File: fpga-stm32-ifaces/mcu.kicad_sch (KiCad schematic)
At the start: 58 parts, among them J10 CORTEX_DEBUG_ETM, J3 PMOD_HOST, J4 XILINX_JTAG, J5 CONN_01X03, U1 STM32H735-UFBGA176-25, U16 W25Q128JV, U2 XC7S25-1FTGB196, U8 AT24MAC402, U9 ECS-1612MV-250-CN

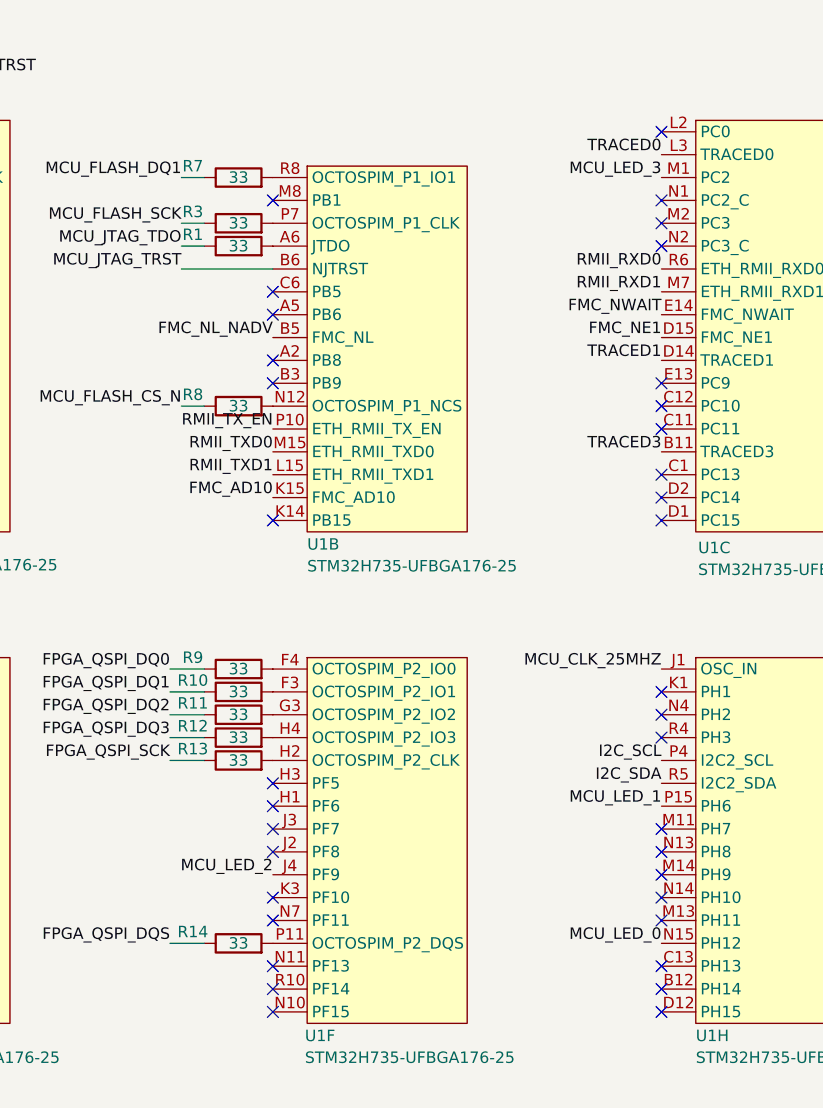
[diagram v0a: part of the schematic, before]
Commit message: Finished initial layout, passing DRC
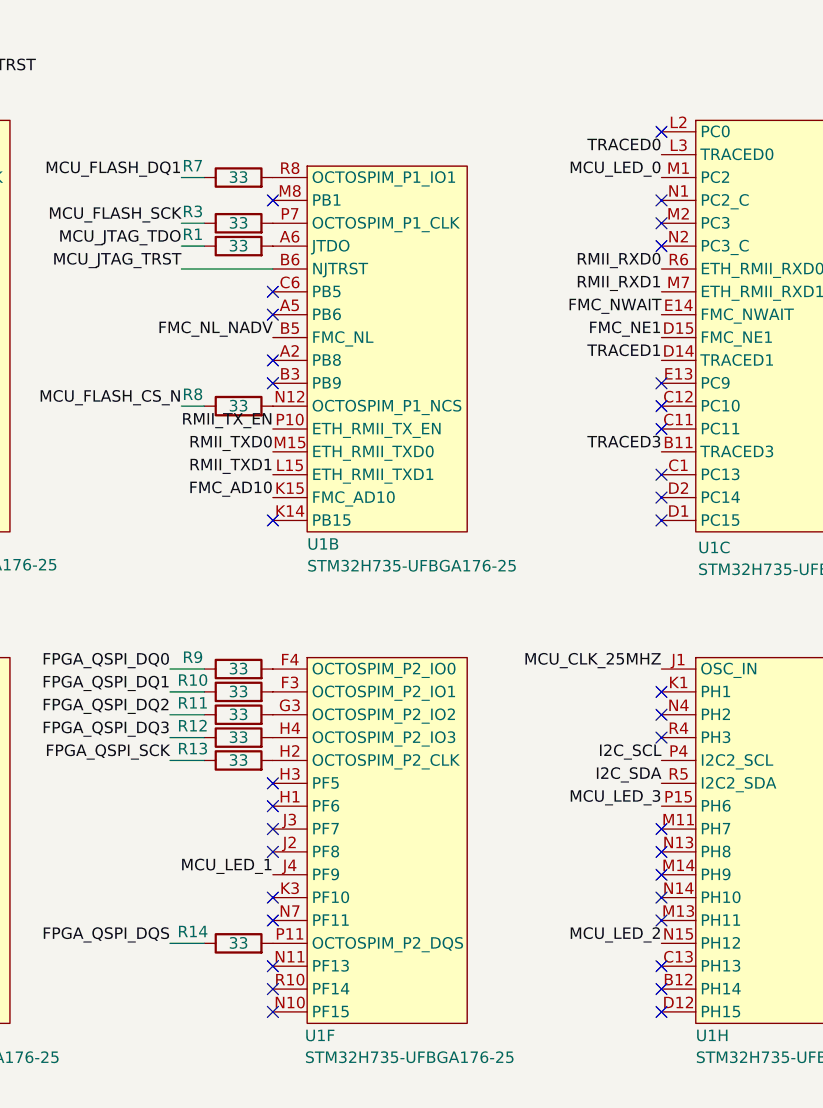
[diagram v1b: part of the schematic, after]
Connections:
- net MCU_LED_0: now also U1.M1 (PC2); no longer U1.N15 (PH12)
- net MCU_LED_1: now also U1.J4 (PF9); no longer U1.P15 (PH6)
- net MCU_LED_2: now also U1.N15 (PH12); no longer U1.J4 (PF9)
- net MCU_LED_3: now also U1.P15 (PH6); no longer U1.M1 (PC2)
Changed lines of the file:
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@@
 	)
 	(label "MCU_LED_2"
-		(at 91.44 113.03 180)
+		(at 134.62 120.65 180)
 		(fields_autoplaced yes)
 		(effects
@@
 	)
 	(label "MCU_LED_3"
-		(at 134.62 35.56 180)
+		(at 134.62 105.41 180)
 		(fields_autoplaced yes)
 		(effects
@@
 	)
 	(label "MCU_LED_0"
-		(at 134.62 120.65 180)
+		(at 134.62 35.56 180)
 		(fields_autoplaced yes)
 		(effects
@@
 	)
 	(label "MCU_LED_1"
-		(at 134.62 105.41 180)
-		(fields_autoplaced yes)
-		(effects
+		(at 91.44 113.03 180)
+		(fields_autoplaced yes)
+		(effects

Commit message: Lots of routing cleanup
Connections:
- net FMC_AD5: now also U2.J4 (IO_L17P_T2_34); no longer U2.J3 (IO_L17N_T2_34)
- net FMC_AD9: now also U2.M5 (IO_L23P_T3_34); no longer U2.K3 (IO_L16N_T2_34)
- net FMC_NL_NADV: now also U2.B2 (IO_L5P_T0_34); no longer U2.C1 (IO_L11N_T1_SRCC_34)
- net FPGA_QSPI_DQ4: now also U2.L5 (IO_25_34); no longer U2.M5 (IO_L23P_T3_34)
- net FPGA_QSPI_DQ5: now also U2.L3 (IO_L22P_T3_34); no longer U2.L5 (IO_25_34)
- net FPGA_QSPI_DQ7: now also U2.C1 (IO_L11N_T1_SRCC_34); no longer U2.B2 (IO_L5P_T0_34)
- net FPGA_QSPI_DQS: now also U2.K4 (IO_L16P_T2_34); no longer U2.L3 (IO_L22P_T3_34)
- net RMII_CRS_DV: now also U2.M4 (IO_L23N_T3_34); no longer U2.K4 (IO_L16P_T2_34)
- net RMII_RXD0: now also U2.K3 (IO_L16N_T2_34); no longer U2.M4 (IO_L23N_T3_34)
- net RMII_RXD1: now also U2.J3 (IO_L17N_T2_34); no longer U2.J4 (IO_L17P_T2_34)
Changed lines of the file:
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@@
 	)
 	(label "FPGA_QSPI_DQS"
-		(at 339.09 146.05 180)
+		(at 339.09 115.57 180)
 		(fields_autoplaced yes)
 		(effects
@@
 	)
 	(label "RMII_RXD1"
-		(at 339.09 120.65 180)
+		(at 339.09 123.19 180)
 		(fields_autoplaced yes)
 		(effects
@@
 	)
 	(label "RMII_RXD0"
-		(at 339.09 153.67 180)
+		(at 339.09 118.11 180)
 		(fields_autoplaced yes)
 		(effects
@@
 	)
 	(label "FMC_AD9"
-		(at 339.09 118.11 180)
+		(at 339.09 151.13 180)
 		(fields_autoplaced yes)
 		(effects
@@
 	)
 	(label "FPGA_QSPI_DQ7"
-		(at 339.09 59.69 180)
+		(at 339.09 92.71 180)
 		(fields_autoplaced yes)
 		(effects
@@
 	)
 	(label "FPGA_QSPI_DQ4"
-		(at 339.09 151.13 180)
+		(at 339.09 161.29 180)
 		(fields_autoplaced yes)
 		(effects
@@
 	)
 	(label "FMC_AD5"
-		(at 339.09 123.19 180)
+		(at 339.09 120.65 180)
 		(fields_autoplaced yes)
 		(effects
@@
 	)
 	(label "RMII_CRS_DV"
-		(at 339.09 115.57 180)
+		(at 339.09 153.67 180)
 		(fields_autoplaced yes)
 		(effects
@@
 	)
 	(label "FPGA_QSPI_DQ5"
-		(at 339.09 161.29 180)
+		(at 339.09 146.05 180)
 		(fields_autoplaced yes)
 		(effects
@@
 	)
 	(label "FMC_NL_NADV"
-		(at 339.09 92.71 180)
-		(fields_autoplaced yes)
-		(effects
+		(at 339.09 59.69 180)
+		(fields_autoplaced yes)
+		(effects

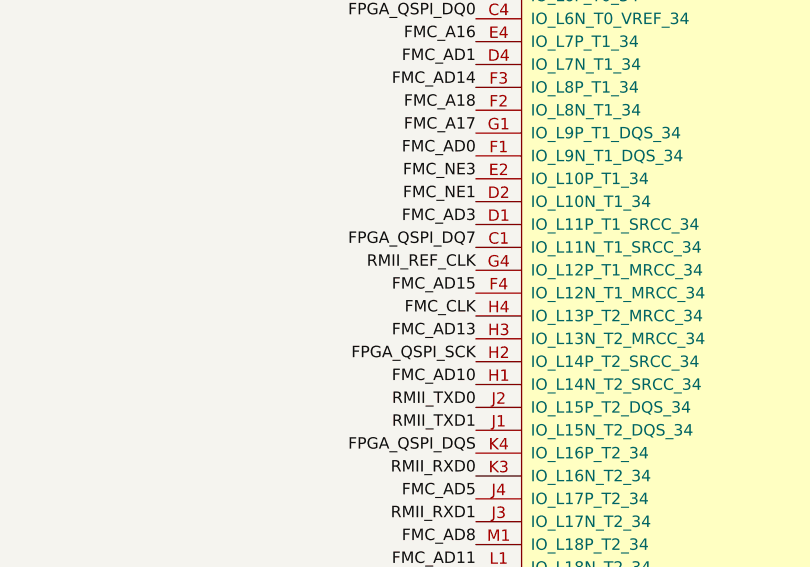
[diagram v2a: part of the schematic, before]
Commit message: More routing cleanup
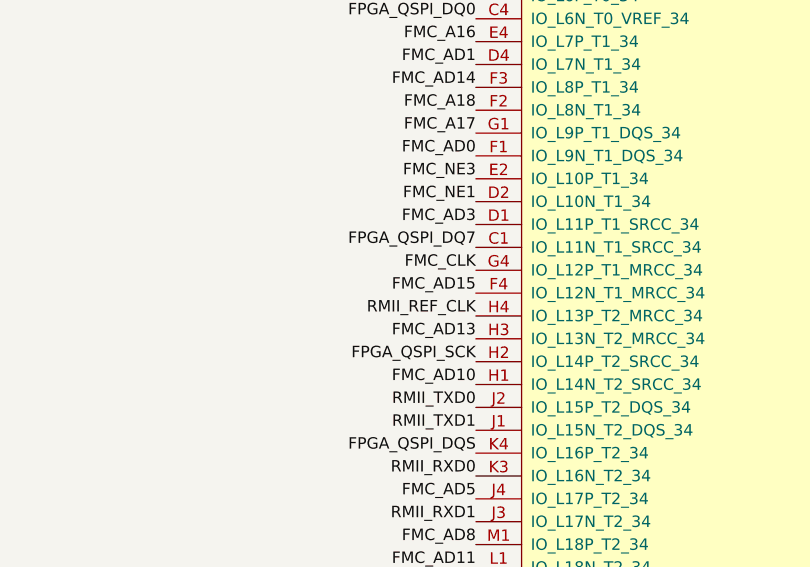
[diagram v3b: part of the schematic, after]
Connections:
- net FMC_CLK: now also U2.G4 (IO_L12P_T1_MRCC_34); no longer U2.H4 (IO_L13P_T2_MRCC_34)
- net RMII_REF_CLK: now also U2.H4 (IO_L13P_T2_MRCC_34); no longer U2.G4 (IO_L12P_T1_MRCC_34)
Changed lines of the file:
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@@
 	)
 	(label "RMII_REF_CLK"
-		(at 339.09 95.25 180)
+		(at 339.09 100.33 180)
 		(fields_autoplaced yes)
 		(effects
@@
 	)
 	(label "FMC_CLK"
-		(at 339.09 100.33 180)
-		(fields_autoplaced yes)
-		(effects
+		(at 339.09 95.25 180)
+		(fields_autoplaced yes)
+		(effects

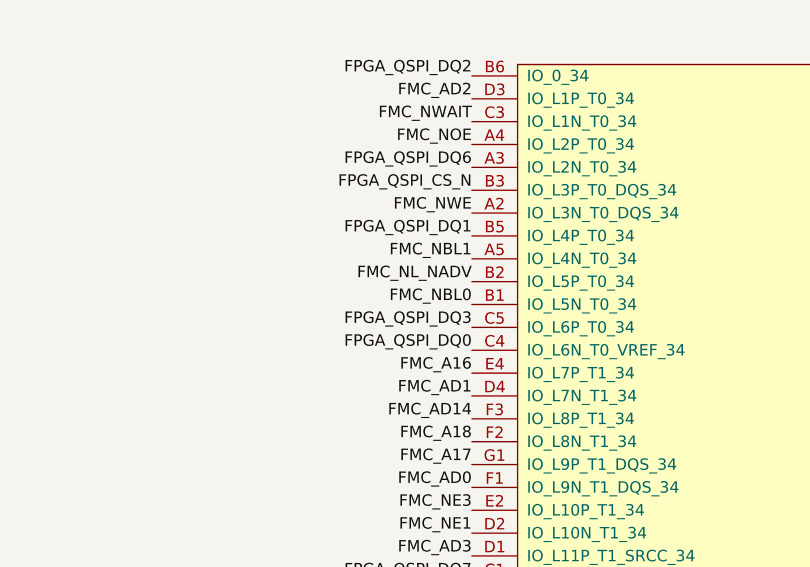
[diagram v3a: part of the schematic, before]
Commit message: More routing cleanup
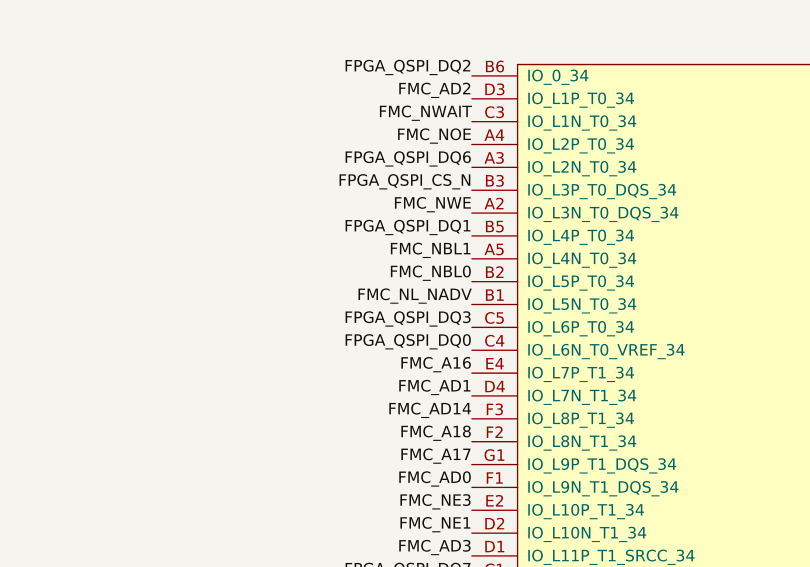
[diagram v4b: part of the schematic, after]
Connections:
- net FMC_NBL0: now also U2.B2 (IO_L5P_T0_34); no longer U2.B1 (IO_L5N_T0_34)
- net FMC_NL_NADV: now also U2.B1 (IO_L5N_T0_34); no longer U2.B2 (IO_L5P_T0_34)
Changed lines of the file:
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@@
 	)
 	(label "FMC_NBL0"
-		(at 339.09 62.23 180)
+		(at 339.09 59.69 180)
 		(fields_autoplaced yes)
 		(effects
@@
 	)
 	(label "FMC_NL_NADV"
-		(at 339.09 59.69 180)
-		(fields_autoplaced yes)
-		(effects
+		(at 339.09 62.23 180)
+		(fields_autoplaced yes)
+		(effects

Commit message: More routing cleanup ready for layout review
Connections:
- net FMC_AD2: now also U2.B3 (IO_L3P_T0_DQS_34); no longer U2.D3 (IO_L1P_T0_34)
- net FMC_AD9: now also U2.M4 (IO_L23N_T3_34); no longer U2.M5 (IO_L23P_T3_34)
- net FMC_NWAIT: now also U2.D3 (IO_L1P_T0_34); no longer U2.C3 (IO_L1N_T0_34)
- net FPGA_QSPI_CS_N: now also U2.C3 (IO_L1N_T0_34); no longer U2.B3 (IO_L3P_T0_DQS_34)
- net RMII_CRS_DV: now also U2.M5 (IO_L23P_T3_34); no longer U2.M4 (IO_L23N_T3_34)
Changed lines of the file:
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@@
 	(title_block
 		(title "FPGA - STM32 Interface Test")
-		(date "2024-06-13")
+		(date "2024-06-18")
 		(rev "0.1")
 		(company "Antikernel Labs")
@@
 	)
 	(label "FMC_NWAIT"
-		(at 339.09 41.91 180)
+		(at 339.09 39.37 180)
 		(fields_autoplaced yes)
 		(effects
@@
 	)
 	(label "FMC_AD9"
-		(at 339.09 151.13 180)
+		(at 339.09 153.67 180)
 		(fields_autoplaced yes)
 		(effects
@@
 	)
 	(label "FPGA_QSPI_CS_N"
-		(at 339.09 49.53 180)
+		(at 339.09 41.91 180)
 		(fields_autoplaced yes)
 		(effects
@@
 	)
 	(label "RMII_CRS_DV"
-		(at 339.09 153.67 180)
+		(at 339.09 151.13 180)
 		(fields_autoplaced yes)
 		(effects
@@
 	)
 	(label "FMC_AD2"
-		(at 339.09 39.37 180)
-		(fields_autoplaced yes)
-		(effects
+		(at 339.09 49.53 180)
+		(fields_autoplaced yes)
+		(effects
